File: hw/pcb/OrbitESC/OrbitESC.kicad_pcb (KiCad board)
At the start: 4 copper layers, 75 x 30 mm, 108 parts, among them J1 USB_C_Receptacle_USB2.0, J2 Micro_SD_Card_Det, J3 TermA, J4 TermB, J5 TermC, J6 CAN1, J7 Serial1, Q1 MCAC80N10Y, Q2 MCAC80N10Y, Q3 MCAC80N10Y, Q4 MCAC80N10Y, Q5 MCAC80N10Y, Q6 MCAC80N10Y, Q7 2N7002, U1 MCP2551-I-SN, U2 AT25SF081-SSHD-X, U3 24LC128, U4 STM32F446ZCHx, U5 DRV8300DRGER, U6 TSV994, U7 AP62200Z6-7, U8 AP2171W, U9 AP2120

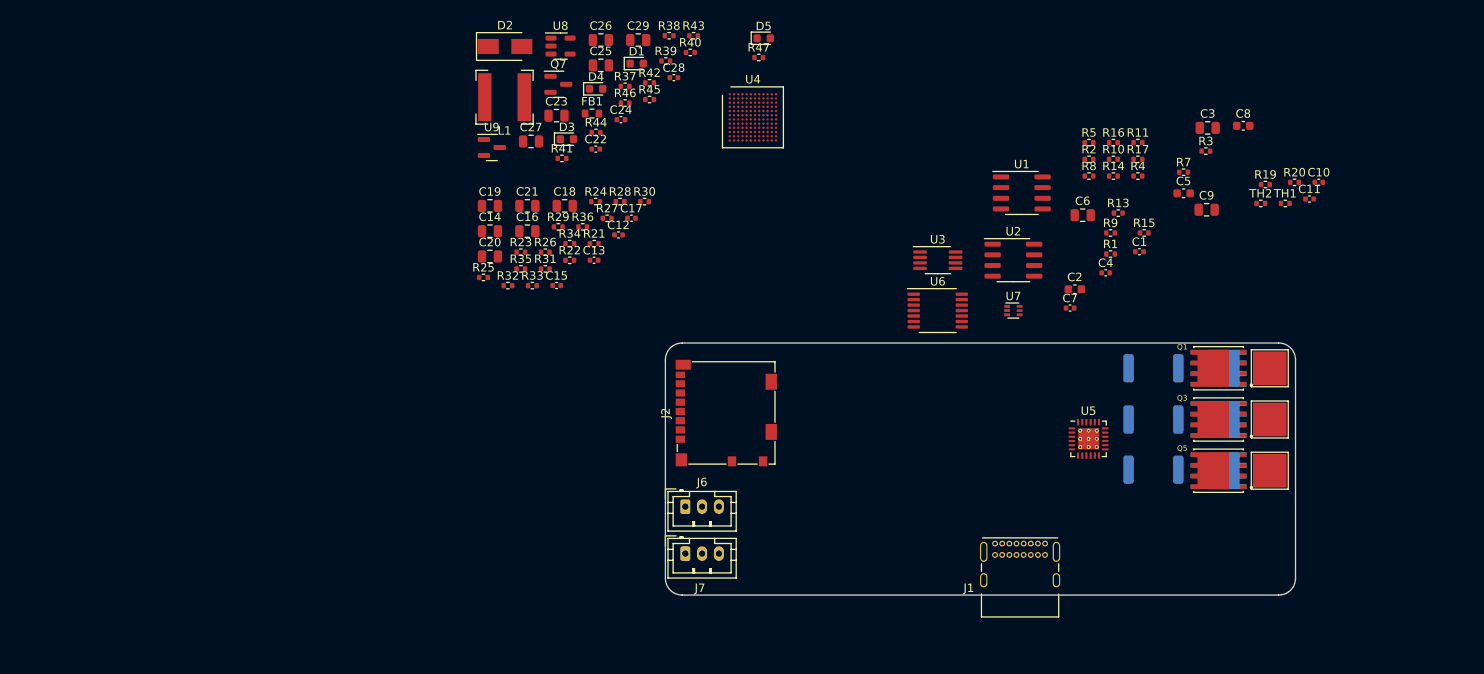
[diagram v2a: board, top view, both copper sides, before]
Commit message: Update PCB to match schematic
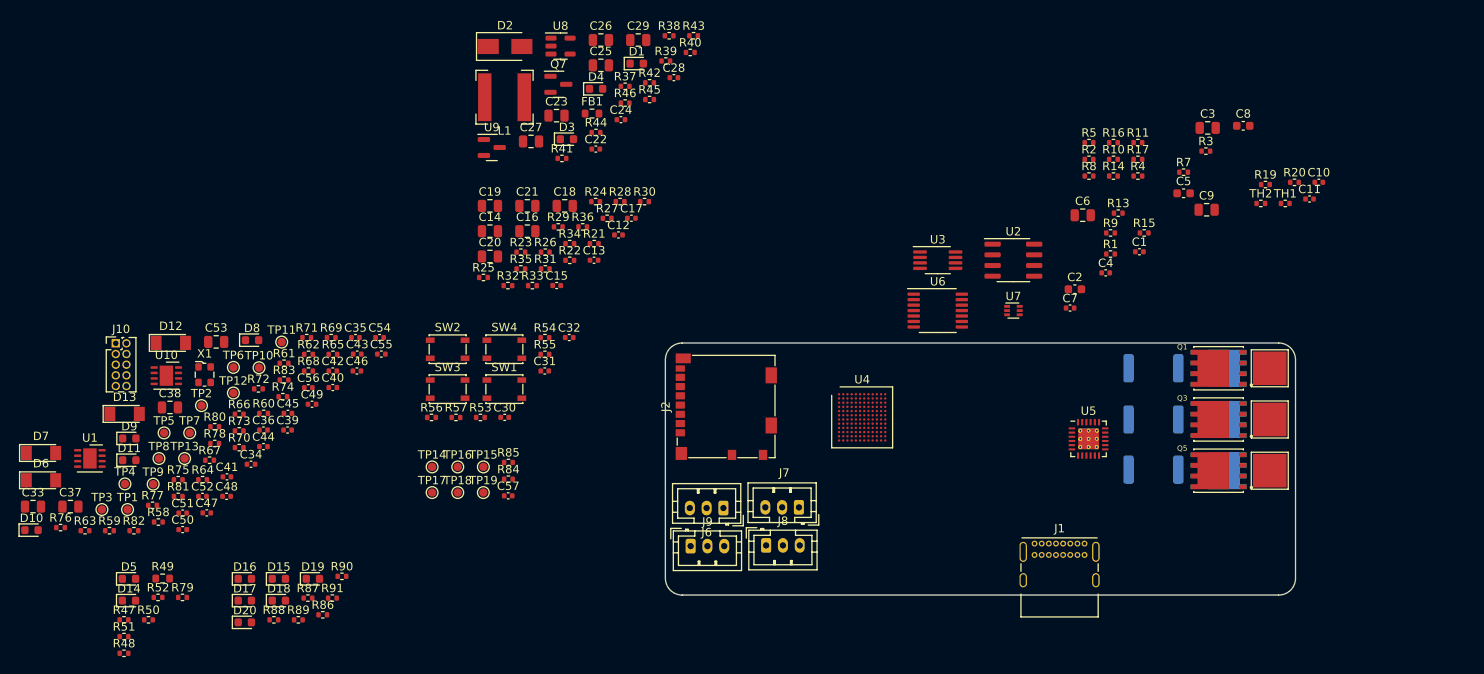
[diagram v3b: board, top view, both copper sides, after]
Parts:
- added C30: 100nF, Capacitor_SMD:C_0402_1005Metric, F.Cu at (84.5, 92.7)
- added C31: 100nF, Capacitor_SMD:C_0402_1005Metric, F.Cu at (89.2, 87.2)
- added C32: 100nF, Capacitor_SMD:C_0402_1005Metric, F.Cu at (92.1, 83.2)
- added C33: 2.2uF, Capacitor_SMD:C_0805_2012Metric, F.Cu at (28.3, 103.3)
- added C34: 100nF, Capacitor_SMD:C_0402_1005Metric, F.Cu at (54.3, 98.3)
- added C35: 100nF, Capacitor_SMD:C_0402_1005Metric, F.Cu at (66.7, 83.2)
- added C36: 100nF, Capacitor_SMD:C_0402_1005Metric, F.Cu at (55.7, 94.2)
- added C37: 2.2uF, Capacitor_SMD:C_0805_2012Metric, F.Cu at (32.8, 103.3)
- added C38: 2.2uF, Capacitor_SMD:C_0805_2012Metric, F.Cu at (44.6, 91.5)
- added C39: 100nF, Capacitor_SMD:C_0402_1005Metric, F.Cu at (58.6, 94.2)
- added C40: 100nF, Capacitor_SMD:C_0402_1005Metric, F.Cu at (64.0, 89.2)
- added C41: 100nF, Capacitor_SMD:C_0402_1005Metric, F.Cu at (51.4, 99.8)
- added C42: 100nF, Capacitor_SMD:C_0402_1005Metric, F.Cu at (64.0, 87.2)
- added C43: 100nF, Capacitor_SMD:C_0402_1005Metric, F.Cu at (66.9, 85.2)
- added C44: 100nF, Capacitor_SMD:C_0402_1005Metric, F.Cu at (55.7, 96.2)
- added C45: 100nF, Capacitor_SMD:C_0402_1005Metric, F.Cu at (58.7, 92.2)
- added C46: 100nF, Capacitor_SMD:C_0402_1005Metric, F.Cu at (66.9, 87.2)
- added C47: 100nF, Capacitor_SMD:C_0402_1005Metric, F.Cu at (49.0, 104.1)
- added C48: 100nF, Capacitor_SMD:C_0402_1005Metric, F.Cu at (51.4, 102.1)
- added C49: 100nF, Capacitor_SMD:C_0402_1005Metric, F.Cu at (61.5, 91.2)
- added C50: 100nF, Capacitor_SMD:C_0402_1005Metric, F.Cu at (46.1, 106.1)
- added C51: 100nF, Capacitor_SMD:C_0402_1005Metric, F.Cu at (46.1, 104.1)
- added C52: 100nF, Capacitor_SMD:C_0402_1005Metric, F.Cu at (48.5, 102.1)
- added C53: 2.2uF, Capacitor_SMD:C_0805_2012Metric, F.Cu at (50.1, 83.7)
- added C54: 100nF, Capacitor_SMD:C_0402_1005Metric, F.Cu at (69.6, 83.2)
- added C55: 100nF, Capacitor_SMD:C_0402_1005Metric, F.Cu at (69.8, 85.2)
- added C56: 100nF, Capacitor_SMD:C_0402_1005Metric, F.Cu at (61.1, 89.2)
- added C57: 100nF, Capacitor_SMD:C_0402_1005Metric, F.Cu at (84.9, 102.0)
- added D10: Yellow LED, Diode_SMD:D_0603_1608Metric, F.Cu at (28.1, 106.1)
- added D11: Yellow LED, Diode_SMD:D_0603_1608Metric, F.Cu at (39.8, 97.8)
- added D12: 3.3V, Diode_SMD:D_MiniMELF, F.Cu at (44.7, 83.8)
- added D13: 3.3V, Diode_SMD:D_MiniMELF, F.Cu at (39.2, 92.3)
- added D14: Yellow LED, Diode_SMD:D_0603_1608Metric, F.Cu at (39.7, 114.5)
- added D15: Green LED, Diode_SMD:D_0603_1608Metric, F.Cu at (57.6, 111.9)
- added D16: Blue LED, Diode_SMD:D_0603_1608Metric, F.Cu at (53.5, 111.9)
- added D17: Blue LED, Diode_SMD:D_0603_1608Metric, F.Cu at (53.5, 114.5)
- added D18: Green LED, Diode_SMD:D_0603_1608Metric, F.Cu at (57.6, 114.5)
- added D19: Blue LED, Diode_SMD:D_0603_1608Metric, F.Cu at (61.6, 111.9)
- added D20: Red LED, Diode_SMD:D_0603_1608Metric, F.Cu at (53.5, 117.1)
- added D6: 3.3V, Diode_SMD:D_MiniMELF, F.Cu at (29.3, 100.2)
- added D7: 3.3V, Diode_SMD:D_MiniMELF, F.Cu at (29.3, 97.0)
- added D8: Yellow LED, Diode_SMD:D_0603_1608Metric, F.Cu at (54.4, 83.5)
- added D9: Yellow LED, Diode_SMD:D_0603_1608Metric, F.Cu at (39.8, 95.2)
- added J10: ~, Connector_PinHeader_1.27mm:PinHeader_2x05_P1.27mm_Vertical, F.Cu at (38.2, 83.9)
- added J8: Serial2, Connector_JST:JST_PH_B3B-PH-K_1x03_P2.00mm_Vertical, F.Cu at (115.6, 108.0)
- added J9: CAN2, Connector_JST:JST_PH_B3B-PH-K_1x03_P2.00mm_Vertical, F.Cu at (106.6, 108.0)
- added R48: 33k, Resistor_SMD:R_0402_1005Metric, F.Cu at (39.1, 120.8)
- added R49: 82k, Resistor_SMD:R_0603_1608Metric, F.Cu at (43.7, 111.9)
- added R50: 1.5k, Resistor_SMD:R_0402_1005Metric, F.Cu at (42.1, 116.8)
- added R51: 5.1k, Resistor_SMD:R_0402_1005Metric, F.Cu at (39.1, 118.8)
- added R52: 5.1k, Resistor_SMD:R_0402_1005Metric, F.Cu at (43.2, 114.1)
- added R53: 10k, Resistor_SMD:R_0402_1005Metric, F.Cu at (81.6, 92.7)
- added R54: 10k, Resistor_SMD:R_0402_1005Metric, F.Cu at (89.2, 83.2)
- added R55: 10k, Resistor_SMD:R_0402_1005Metric, F.Cu at (89.2, 85.2)
- added R56: 10k, Resistor_SMD:R_0402_1005Metric, F.Cu at (75.7, 92.7)
- added R57: 10k, Resistor_SMD:R_0402_1005Metric, F.Cu at (78.7, 92.7)
- added R58: 1.5k, Resistor_SMD:R_0402_1005Metric, F.Cu at (43.2, 105.2)
- added R59: 1.5k, Resistor_SMD:R_0402_1005Metric, F.Cu at (37.4, 106.2)
- added R60: 1.5k, Resistor_SMD:R_0402_1005Metric, F.Cu at (55.8, 92.2)
- added R61: 1.5k, Resistor_SMD:R_0402_1005Metric, F.Cu at (58.2, 86.3)
- added R62: 120, Resistor_SMD:R_0402_1005Metric, F.Cu at (61.1, 85.2)
- added R63: 120, Resistor_SMD:R_0402_1005Metric, F.Cu at (34.5, 106.2)
- added R64: 1.5k, Resistor_SMD:R_0402_1005Metric, F.Cu at (48.5, 100.1)
- added R65: 1.5k, Resistor_SMD:R_0402_1005Metric, F.Cu at (64.0, 85.2)
- added R66: 1.5k, Resistor_SMD:R_0402_1005Metric, F.Cu at (52.9, 92.3)
- added R67: 1.5k, Resistor_SMD:R_0402_1005Metric, F.Cu at (49.3, 97.8)
- added R68: 1.5k, Resistor_SMD:R_0402_1005Metric, F.Cu at (61.1, 87.2)
- added R69: 10k, Resistor_SMD:R_0402_1005Metric, F.Cu at (63.8, 83.2)
- added R70: 10k, Resistor_SMD:R_0402_1005Metric, F.Cu at (52.9, 96.3)
- added R71: 10k, Resistor_SMD:R_0402_1005Metric, F.Cu at (60.9, 83.2)
- added R72: 39k, Resistor_SMD:R_0402_1005Metric, F.Cu at (55.1, 89.3)
- added R73: 39k, Resistor_SMD:R_0402_1005Metric, F.Cu at (52.9, 94.3)
- added R74: 39k, Resistor_SMD:R_0402_1005Metric, F.Cu at (58.1, 90.2)
- added R75: 39k, Resistor_SMD:R_0402_1005Metric, F.Cu at (45.6, 100.1)
- added R76: 39k, Resistor_SMD:R_0402_1005Metric, F.Cu at (31.6, 105.8)
- added R77: 1.5k, Resistor_SMD:R_0402_1005Metric, F.Cu at (42.5, 103.2)
- added R78: 1.5k, Resistor_SMD:R_0402_1005Metric, F.Cu at (49.9, 95.8)
- added R79: 1.5k, Resistor_SMD:R_0402_1005Metric, F.Cu at (46.1, 114.1)
- added R80: 100k, Resistor_SMD:R_0402_1005Metric, F.Cu at (49.9, 93.8)
- added R81: 100k, Resistor_SMD:R_0402_1005Metric, F.Cu at (45.6, 102.1)
- added R82: 100k, Resistor_SMD:R_0402_1005Metric, F.Cu at (40.3, 106.2)
- added R83: 100k, Resistor_SMD:R_0402_1005Metric, F.Cu at (58.2, 88.3)
- added R84: 10k, Resistor_SMD:R_0402_1005Metric, F.Cu at (84.9, 100.1)
- added R85: 10k, Resistor_SMD:R_0402_1005Metric, F.Cu at (84.9, 98.1)
- added R86: 10k, Resistor_SMD:R_0402_1005Metric, F.Cu at (62.8, 116.2)
- added R87: 200, Resistor_SMD:R_0402_1005Metric, F.Cu at (61.0, 114.2)
- added R88: 200, Resistor_SMD:R_0402_1005Metric, F.Cu at (57.0, 116.8)
- added R89: 10k, Resistor_SMD:R_0402_1005Metric, F.Cu at (59.9, 116.8)
- added R90: 200, Resistor_SMD:R_0402_1005Metric, F.Cu at (65.1, 111.6)
- added R91: 1.5k, Resistor_SMD:R_0402_1005Metric, F.Cu at (63.9, 114.2)
- added SW1: Reset, Button_Switch_SMD:SW_SPST_PTS810, F.Cu at (84.4, 89.3)
- added SW2: User, Button_Switch_SMD:SW_SPST_PTS810, F.Cu at (77.7, 84.6)
- added SW3: Boot, Button_Switch_SMD:SW_SPST_PTS810, F.Cu at (77.7, 89.3)
- added SW4: Break, Button_Switch_SMD:SW_SPST_PTS810, F.Cu at (84.4, 84.6)
- added TP1: SDIO_CMD, TestPoint:TestPoint_Pad_D1.0mm, F.Cu at (39.6, 103.7)
- added TP10: NOR_SCK, TestPoint:TestPoint_Pad_D1.0mm, F.Cu at (55.2, 86.8)
- added TP11: EEPROM_SDA, TestPoint:TestPoint_Pad_D1.0mm, F.Cu at (57.9, 83.8)
- added TP12: EEPROM_SCL, TestPoint:TestPoint_Pad_D1.0mm, F.Cu at (52.2, 89.8)
- added TP13: NOR_MISO, TestPoint:TestPoint_Pad_D1.0mm, F.Cu at (46.4, 97.6)
- added TP14: AH, TestPoint:TestPoint_Pad_D1.0mm, F.Cu at (75.8, 98.6)
- added TP15: AL, TestPoint:TestPoint_Pad_D1.0mm, F.Cu at (81.9, 98.6)
- added TP16: BH, TestPoint:TestPoint_Pad_D1.0mm, F.Cu at (78.9, 98.6)
- added TP17: BL, TestPoint:TestPoint_Pad_D1.0mm, F.Cu at (75.8, 101.7)
- added TP18: CH, TestPoint:TestPoint_Pad_D1.0mm, F.Cu at (78.9, 101.7)
- added TP19: CL, TestPoint:TestPoint_Pad_D1.0mm, F.Cu at (81.9, 101.7)
- added TP2: SDIO_DATA_2, TestPoint:TestPoint_Pad_D1.0mm, F.Cu at (48.4, 91.3)
- added TP3: SDIO_DATA_0, TestPoint:TestPoint_Pad_D1.0mm, F.Cu at (36.5, 103.7)
- added TP4: SDIO_CARD_DETECT, TestPoint:TestPoint_Pad_D1.0mm, F.Cu at (39.3, 100.6)
- added TP5: NOR_nCS, TestPoint:TestPoint_Pad_D1.0mm, F.Cu at (43.9, 94.6)
- added TP6: SDIO_DATA_3, TestPoint:TestPoint_Pad_D1.0mm, F.Cu at (52.2, 86.8)
- added TP7: SDIO_CLK, TestPoint:TestPoint_Pad_D1.0mm, F.Cu at (47.0, 94.6)
- added TP8: SDIO_DATA_1, TestPoint:TestPoint_Pad_D1.0mm, F.Cu at (43.3, 97.6)
- added TP9: NOR_MOSI, TestPoint:TestPoint_Pad_D1.0mm, F.Cu at (42.6, 100.7)
- added U10: TLE9250X, Package_SON:HVSON-8-1EP_3x3mm_P0.65mm_EP1.6x2.4mm, F.Cu at (44.2, 87.8)
- added X1: ECS-2520MV-240-BN, Oscillator:Oscillator_SMD_ECS_2520MV-xxx-xx-4Pin_2.5x2.0mm, F.Cu at (48.7, 87.6)
- U1: value MCP2551-I-SN -> TLE9250X; footprint Package_SO:SOIC-8_3.9x4.9mm_P1.27mm -> Package_SON:HVSON-8-1EP_3x3mm_P0.65mm_EP1.6x2.4mm
- moved U1 115.3 mm to (35.1, 97.6)
- moved R47 100.9 mm to (39.1, 116.8)
- moved D5 99.2 mm to (39.7, 111.9)
- moved U4 38.0 mm to (127.0, 92.7)
- moved J7 14.6 mm to (119.5, 103.4), turned to 180 degrees
- moved J1 4.70 mm to (147.5, 107.7)
- moved J6 4.54 mm to (110.5, 103.5), turned to 180 degrees
- moved J2 0.76 mm to (110.8, 91.4)
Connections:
- C1 pad 1: /Outputs and Shunts/VA_FB -> /MCU/MOTOR_VA
- C10 pad 1: /Outputs and Shunts/TempA -> /MCU/TEMP_VA
- C10 pad 2: GNDD -> GND
- C11 pad 1: /Outputs and Shunts/TempB -> /MCU/TEMP_VB
- C11 pad 2: GNDD -> GND
- C13 pad 1: /Power Stage/VS -> /MCU/INPUT_VOLTAGE
- C13 pad 2: GNDD -> GND
- C15 pad 1: /Power Stage/VL -> /MCU/+3V3_VOLTAGE
- C15 pad 2: GNDD -> GND
- C22 pad 1: GNDD -> GND
- C23 pad 2: GNDD -> GND
- C25 pad 2: GNDD -> GND
- C26 pad 2: GNDD -> GND
- C27 pad 1: GNDD -> GND
- C28 pad 2: GNDD -> GND
- C29 pad 1: GNDD -> GND
- C4 pad 1: /Outputs and Shunts/VB_FB -> /MCU/MOTOR_VB
- C7 pad 1: /Outputs and Shunts/VC_FB -> /MCU/MOTOR_VC
- D1 pad 1: GNDD -> GND
- D2 pad 2: GNDD -> GND
- D3 pad 1: GNDD -> GND
- D4 pad 1: GNDD -> GND
- D5 pad 1: unconnected-(D5-Pad1) -> GND
- D5 pad 2: unconnected-(D5-Pad2) -> Net-(D5-Pad2)
- J1 pad A1: Net-(J1-PadA1) -> GND
- J1 pad A12: Net-(J1-PadA1) -> GND
- J1 pad A4: Net-(J1-PadA4) -> VBUS
- J1 pad A5: unconnected-(J1-PadA5) -> Net-(J1-PadA5)
- J1 pad A6: unconnected-(J1-PadA6) -> USB_D+
- J1 pad A7: unconnected-(J1-PadA7) -> USB_D-
- J1 pad A9: Net-(J1-PadA4) -> VBUS
- J1 pad B1: Net-(J1-PadA1) -> GND
- J1 pad B12: Net-(J1-PadA1) -> GND
- J1 pad B4: Net-(J1-PadA4) -> VBUS
- J1 pad B5: unconnected-(J1-PadB5) -> Net-(J1-PadB5)
- J1 pad B6: unconnected-(J1-PadB6) -> USB_D+
- J1 pad B7: unconnected-(J1-PadB7) -> USB_D-
- J1 pad B9: Net-(J1-PadA4) -> VBUS
- J1 pad S1: unconnected-(J1-PadS1) -> GND
- J2 pad 1: unconnected-(J2-Pad1) -> SDIO_DATA_2
- J2 pad 10: unconnected-(J2-Pad10) -> SDIO_CARD_DETECT
- J2 pad 11: unconnected-(J2-Pad11) -> GND
- J2 pad 2: unconnected-(J2-Pad2) -> SDIO_DATA_3
- J2 pad 3: unconnected-(J2-Pad3) -> SDIO_CMD
- J2 pad 4: unconnected-(J2-Pad4) -> +3.3V
- J2 pad 5: unconnected-(J2-Pad5) -> SDIO_CLK
- J2 pad 6: unconnected-(J2-Pad6) -> GND
- J2 pad 7: unconnected-(J2-Pad7) -> SDIO_DATA_0
- J2 pad 8: unconnected-(J2-Pad8) -> SDIO_DATA_1
- J2 pad 9: unconnected-(J2-Pad9) -> GND
- J6 pad 1: unconnected-(J6-Pad1) -> Net-(J6-Pad1)
- J6 pad 2: unconnected-(J6-Pad2) -> GND
- J6 pad 3: unconnected-(J6-Pad3) -> Net-(J6-Pad3)
- J7 pad 1: unconnected-(J7-Pad1) -> Net-(D6-Pad1)
- J7 pad 2: unconnected-(J7-Pad2) -> Net-(D12-Pad1)
- J7 pad 3: unconnected-(J7-Pad3) -> GND
- Q7 pad 2: GNDD -> GND
- R1 pad 2: /Outputs and Shunts/VA_FB -> /MCU/MOTOR_VA
- R13 pad 2: /Outputs and Shunts/VB_FB -> /MCU/MOTOR_VB
- R15 pad 1: /Outputs and Shunts/VB_FB -> /MCU/MOTOR_VB
- R19 pad 2: /Outputs and Shunts/VC_FB -> /MCU/MOTOR_VC
- R20 pad 1: /Outputs and Shunts/VC_FB -> /MCU/MOTOR_VC
- R23 pad 1: /Power Stage/VS -> /MCU/INPUT_VOLTAGE
- R24 pad 1: /Power Stage/VS -> /MCU/INPUT_VOLTAGE
- R24 pad 2: GNDD -> GND
- R25 pad 1: /Power Stage/IC -> /MCU/MOTOR_IC
- R27 pad 2: Net-(U6-Pad3) -> ISenseVRef
- R29 pad 1: /Power Stage/VL -> /MCU/+3V3_VOLTAGE
- R3 pad 1: /Outputs and Shunts/VA_FB -> /MCU/MOTOR_VA
- R30 pad 1: GNDD -> GND
- R30 pad 2: /Power Stage/VL -> /MCU/+3V3_VOLTAGE
- R31 pad 1: /Power Stage/IB -> /MCU/MOTOR_IB
- R33 pad 2: Net-(U6-Pad10) -> ISenseVRef
- R34 pad 1: /Power Stage/IA -> /MCU/MOTOR_IA
- R36 pad 2: Net-(U6-Pad5) -> ISenseVRef
- R38 pad 1: GNDD -> GND
- R41 pad 1: GNDD -> GND
- R47 pad 1: unconnected-(R47-Pad1) -> VBUS
- R47 pad 2: unconnected-(R47-Pad2) -> Net-(D5-Pad2)
- R7 pad 1: /Outputs and Shunts/TempA -> /MCU/TEMP_VA
- R7 pad 2: GNDD -> GND
- R9 pad 1: /Outputs and Shunts/TempB -> /MCU/TEMP_VB
- R9 pad 2: GNDD -> GND
- TH1 pad 2: /Outputs and Shunts/TempA -> /MCU/TEMP_VA
- TH2 pad 2: /Outputs and Shunts/TempB -> /MCU/TEMP_VB
- U1 pad 1: unconnected-(U1-Pad1) -> CAN1_TXD
- U1 pad 2: unconnected-(U1-Pad2) -> GND
- U1 pad 3: unconnected-(U1-Pad3) -> +5V
- U1 pad 4: unconnected-(U1-Pad4) -> CAN1_RXD
- U1 pad 5: unconnected-(U1-Pad5) -> +3.3V
- U1 pad 6: unconnected-(U1-Pad6) -> Net-(J6-Pad3)
- U1 pad 7: unconnected-(U1-Pad7) -> Net-(J6-Pad1)
- U2 pad 1: unconnected-(U2-Pad1) -> NOR_nCS
- U2 pad 2: unconnected-(U2-Pad2) -> NOR_MISO
- U2 pad 3: unconnected-(U2-Pad3) -> +3.3V
- U2 pad 4: unconnected-(U2-Pad4) -> GND
- U2 pad 5: unconnected-(U2-Pad5) -> NOR_MOSI
- U2 pad 6: unconnected-(U2-Pad6) -> NOR_SCK
- U2 pad 7: unconnected-(U2-Pad7) -> +3.3V
- U2 pad 8: unconnected-(U2-Pad8) -> +3.3V
- U3 pad 1: unconnected-(U3-Pad1) -> GND
- U3 pad 2: unconnected-(U3-Pad2) -> GND
- U3 pad 3: unconnected-(U3-Pad3) -> GND
- U3 pad 4: unconnected-(U3-Pad4) -> GND
- U3 pad 5: unconnected-(U3-Pad5) -> EEPROM_SDA
- U3 pad 6: unconnected-(U3-Pad6) -> EEPROM_SCL
- U3 pad 7: unconnected-(U3-Pad7) -> GND
- U3 pad 8: unconnected-(U3-Pad8) -> +3.3V
- U4 pad A1: unconnected-(U4-PadA1) -> HEARTBEAT_LED
- U4 pad A10: unconnected-(U4-PadA10) -> JTAG_TDI
- U4 pad A11: unconnected-(U4-PadA11) -> JTAG_TCLK
- U4 pad A12: unconnected-(U4-PadA12) -> JTAG_TMS
- U4 pad A2: unconnected-(U4-PadA2) -> USER_BTN
- U4 pad A3: unconnected-(U4-PadA3) -> FAULT_LED
- U4 pad A4: unconnected-(U4-PadA4) -> ARMED_LED
- U4 pad A5: unconnected-(U4-PadA5) -> CAN1_ACTV_LED
- U4 pad A7: unconnected-(U4-PadA7) -> JTAG_TDO
- U4 pad A8: unconnected-(U4-PadA8) -> SERIAL1_IN
- U4 pad B10: unconnected-(U4-PadB10) -> SDIO_DATA_3
- U4 pad B11: unconnected-(U4-PadB11) -> SDIO_DATA_2
- U4 pad B12: unconnected-(U4-PadB12) -> USB_D+
- U4 pad B2: unconnected-(U4-PadB2) -> STATUS_0_LED
- U4 pad B3: unconnected-(U4-PadB3) -> STATUS_1_LED
- U4 pad B4: unconnected-(U4-PadB4) -> STATUS_2_LED
- U4 pad B5: unconnected-(U4-PadB5) -> CAN1_TXD
- U4 pad B6: unconnected-(U4-PadB6) -> CAN2_RXD
- U4 pad B7: unconnected-(U4-PadB7) -> CAN2_ACTV_LED
- U4 pad B8: unconnected-(U4-PadB8) -> SERIAL1_ACTV_LED
- U4 pad B9: unconnected-(U4-PadB9) -> SERIAL1_OUT
- U4 pad C10: unconnected-(U4-PadC10) -> SDIO_CLK
- U4 pad C11: unconnected-(U4-PadC11) -> +3.3V
- U4 pad C12: unconnected-(U4-PadC12) -> USB_D-
- U4 pad C2: unconnected-(U4-PadC2) -> +3.3V
- U4 pad C3: unconnected-(U4-PadC3) -> EEPROM_SDA
- U4 pad C4: unconnected-(U4-PadC4) -> EEPROM_SCL
- U4 pad C5: unconnected-(U4-PadC5) -> CAN1_RXD
- U4 pad C6: unconnected-(U4-PadC6) -> CAN2_TXD
- U4 pad C7: unconnected-(U4-PadC7) -> SERIAL2_OUT
- U4 pad D1: unconnected-(U4-PadD1) -> OSC
- U4 pad D10: unconnected-(U4-PadD10) -> SDIO_CARD_DETECT
- U4 pad D11: unconnected-(U4-PadD11) -> USB_ACTV_LED
- U4 pad D12: unconnected-(U4-PadD12) -> USB_Detect
- U4 pad D2: unconnected-(U4-PadD2) -> GND
- U4 pad D3: unconnected-(U4-PadD3) -> +3.3V
- U4 pad D5: unconnected-(U4-PadD5) -> BOOT0
- U4 pad D7: unconnected-(U4-PadD7) -> SERIAL2_ACTV_LED
- U4 pad E11: unconnected-(U4-PadE11) -> SDIO_DATA_1
- U4 pad E12: unconnected-(U4-PadE12) -> USB_ENUM
- U4 pad E2: unconnected-(U4-PadE2) -> /MCU/TEMP_VA
- U4 pad E5: unconnected-(U4-PadE5) -> +3.3V
- U4 pad E6: unconnected-(U4-PadE6) -> GND
- U4 pad E7: unconnected-(U4-PadE7) -> GND
- U4 pad E8: unconnected-(U4-PadE8) -> SERIAL2_IN
- U4 pad E9: unconnected-(U4-PadE9) -> SDIO_CMD
- U4 pad F1: unconnected-(U4-PadF1) -> nRESET
- U4 pad F10: unconnected-(U4-PadF10) -> +3.3V
- U4 pad F11: unconnected-(U4-PadF11) -> SDIO_DATA_0
- U4 pad F4: unconnected-(U4-PadF4) -> +3.3V
- U4 pad F5: unconnected-(U4-PadF5) -> +3.3V
- U4 pad F6: unconnected-(U4-PadF6) -> +3.3V
- U4 pad F7: unconnected-(U4-PadF7) -> +3.3V
- U4 pad F8: unconnected-(U4-PadF8) -> +3.3V
- U4 pad F9: unconnected-(U4-PadF9) -> +3.3V
- U4 pad G1: unconnected-(U4-PadG1) -> /MCU/+3V3_VOLTAGE
- U4 pad G10: unconnected-(U4-PadG10) -> GND
- U4 pad G2: unconnected-(U4-PadG2) -> /MCU/TEMP_VB
- U4 pad G4: unconnected-(U4-PadG4) -> GND
- U4 pad G5: unconnected-(U4-PadG5) -> +3.3V
- U4 pad G6: unconnected-(U4-PadG6) -> +3.3V
- U4 pad G7: unconnected-(U4-PadG7) -> +3.3V
- U4 pad G8: unconnected-(U4-PadG8) -> GND
- U4 pad G9: unconnected-(U4-PadG9) -> Net-(C38-Pad2)
- U4 pad H1: unconnected-(U4-PadH1) -> /MCU/+5V0_VOLTAGE
- U4 pad H5: unconnected-(U4-PadH5) -> Net-(R69-Pad2)
- U4 pad H6: unconnected-(U4-PadH6) -> GND
- U4 pad H7: unconnected-(U4-PadH7) -> Net-(C37-Pad2)
- U4 pad H8: unconnected-(U4-PadH8) -> /MCU/GATE_DRIVE_BH
- U4 pad J1: unconnected-(U4-PadJ1) -> GND
- U4 pad J2: unconnected-(U4-PadJ2) -> /MCU/INPUT_VOLTAGE
- U4 pad J3: unconnected-(U4-PadJ3) -> /MCU/MOTOR_VA
- U4 pad J5: unconnected-(U4-PadJ5) -> BOOT1
- U4 pad J7: unconnected-(U4-PadJ7) -> /MCU/GATE_DRIVE_BL
- U4 pad J8: unconnected-(U4-PadJ8) -> /MCU/GATE_DRIVE_CL
- U4 pad K1: unconnected-(U4-PadK1) -> GND
- U4 pad K2: unconnected-(U4-PadK2) -> /MCU/MOTOR_IA
- U4 pad K3: unconnected-(U4-PadK3) -> /MCU/MOTOR_VB
- U4 pad K7: unconnected-(U4-PadK7) -> /MCU/GATE_DRIVE_AH
- U4 pad K8: unconnected-(U4-PadK8) -> /MCU/GATE_DRIVE_CH
- U4 pad L1: unconnected-(U4-PadL1) -> +3.3VADC
- U4 pad L11: unconnected-(U4-PadL11) -> NOR_MISO
- U4 pad L12: unconnected-(U4-PadL12) -> NOR_MOSI
- U4 pad L2: unconnected-(U4-PadL2) -> /MCU/MOTOR_IB
- U4 pad L3: unconnected-(U4-PadL3) -> /MCU/MOTOR_VC
- U4 pad L7: unconnected-(U4-PadL7) -> /MCU/GATE_DRIVE_AL
- U4 pad M1: unconnected-(U4-PadM1) -> +3.3VADC
- U4 pad M11: unconnected-(U4-PadM11) -> NOR_nCS
- U4 pad M12: unconnected-(U4-PadM12) -> NOR_SCK
- U4 pad M2: unconnected-(U4-PadM2) -> /MCU/MOTOR_IC
- U4 pad M8: unconnected-(U4-PadM8) -> TIM1_BREAK
- U5 pad 1: /Power Stage/AL -> /MCU/GATE_DRIVE_AL
- U5 pad 2: /Power Stage/BL -> /MCU/GATE_DRIVE_BL
- U5 pad 22: /Power Stage/AH -> /MCU/GATE_DRIVE_AH
- U5 pad 23: /Power Stage/BH -> /MCU/GATE_DRIVE_BH
- U5 pad 24: /Power Stage/CH -> /MCU/GATE_DRIVE_CH
- U5 pad 25: (no net) -> GND
- U5 pad 3: /Power Stage/CL -> /MCU/GATE_DRIVE_CL
- U5 pad 7: (no net) -> unconnected-(U5-Pad7)
- U5 pad 8: (no net) -> unconnected-(U5-Pad8)
- U6 pad 1: /Power Stage/IC -> /MCU/MOTOR_IC
- U6 pad 10: Net-(U6-Pad10) -> ISenseVRef
- U6 pad 3: Net-(U6-Pad3) -> ISenseVRef
- U6 pad 5: Net-(U6-Pad5) -> ISenseVRef
- U6 pad 7: /Power Stage/IA -> /MCU/MOTOR_IA
- U6 pad 8: /Power Stage/IB -> /MCU/MOTOR_IB
- U7 pad 3: GNDD -> GND
- U8 pad 2: GNDD -> GND
- U9 pad 1: GNDD -> GND

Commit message: Start routing power stage
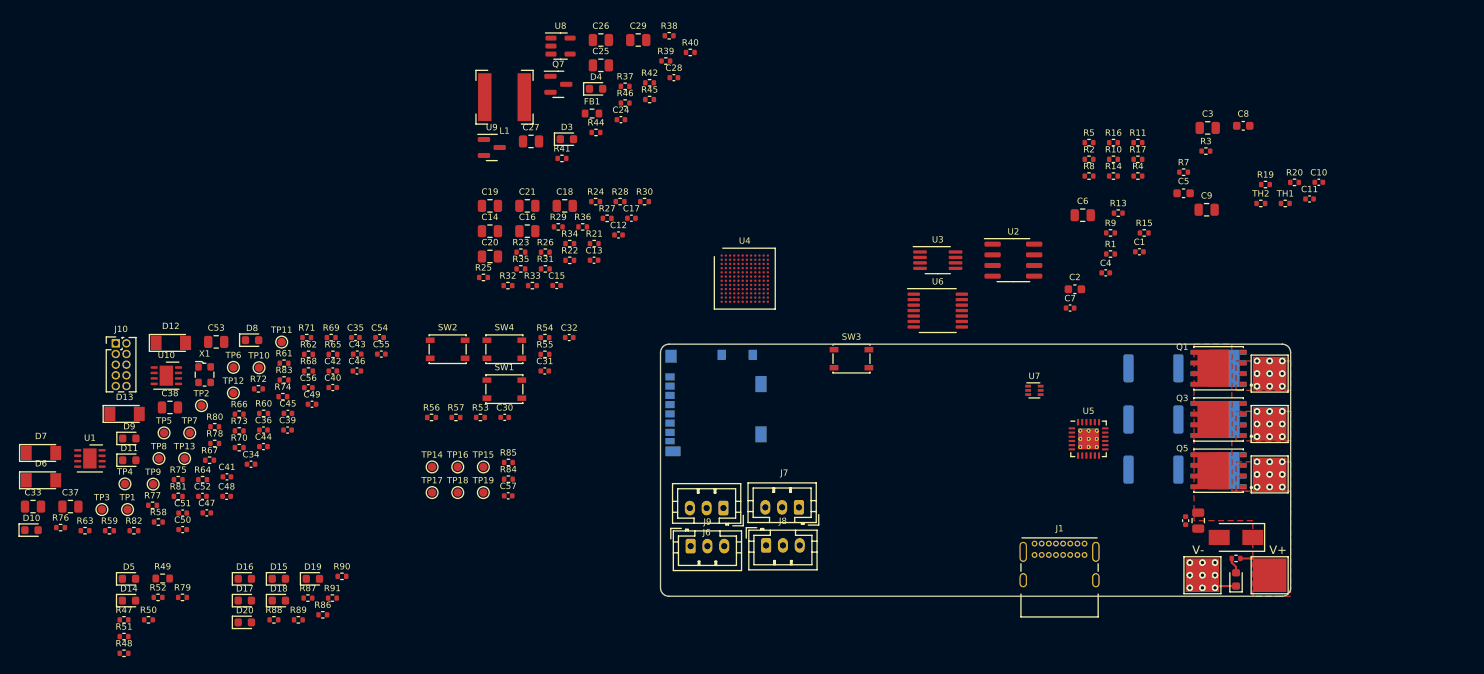
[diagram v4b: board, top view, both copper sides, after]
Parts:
- added J11: VDC, TestPoint:TestPoint_Pad_4.0x4.0mm, F.Cu at (175.5, 111.5)
- added J12: GND, TestPoint:TestPoint_Pad_4.0x4.0mm, F.Cu at (167.5, 111.5)
- J2: moved to B.Cu
- moved D2 104.8 mm to (171.5, 107.0), turned to 180 degrees
- moved D1 94.1 mm to (171.5, 112.0), turned to 90 degrees
- moved C23 90.3 mm to (167.0, 105.0), turned to -90 degrees
- moved R43 89.7 mm to (171.5, 109.5), turned to 180 degrees
- moved C22 83.0 mm to (165.5, 105.0), turned to 90 degrees
- moved SW3 48.2 mm to (125.7, 85.7)
- moved U4 21.6 mm to (113.0, 76.2)
- moved U7 9.82 mm to (147.5, 89.5)
- moved J2 1.30 mm to (109.6, 91.0), turned to -90 degrees
- moved J3 0.63 mm to (175.5, 87.5)
- moved J4 0.54 mm to (175.5, 93.5)
- moved J5 0.44 mm to (175.5, 99.5)
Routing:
- net VDC: track 0.00 -> 4.32 mm
- net GND: track 0.00 -> 2.59 mm, vias 0 -> 9
- net Net-(D1-Pad2): track 0.00 -> 1.92 mm
- net /Outputs and Shunts/SH_C: vias 0 -> 9
- net /Outputs and Shunts/SH_B: vias 0 -> 9
- net /Outputs and Shunts/SH_A: vias 0 -> 9
- added copper zone on F.Cu, net /Outputs and Shunts/SH_A
- added copper zone on F.Cu, net /Outputs and Shunts/SH_B
- added copper zone on F.Cu, net /Outputs and Shunts/SH_C
- added copper zone on In1.Cu, net GND
- added copper zone on F.Cu, net VDC
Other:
- outline, holes or cut-outs redrawn
- board text added: "V+"
- board text added: "V-"

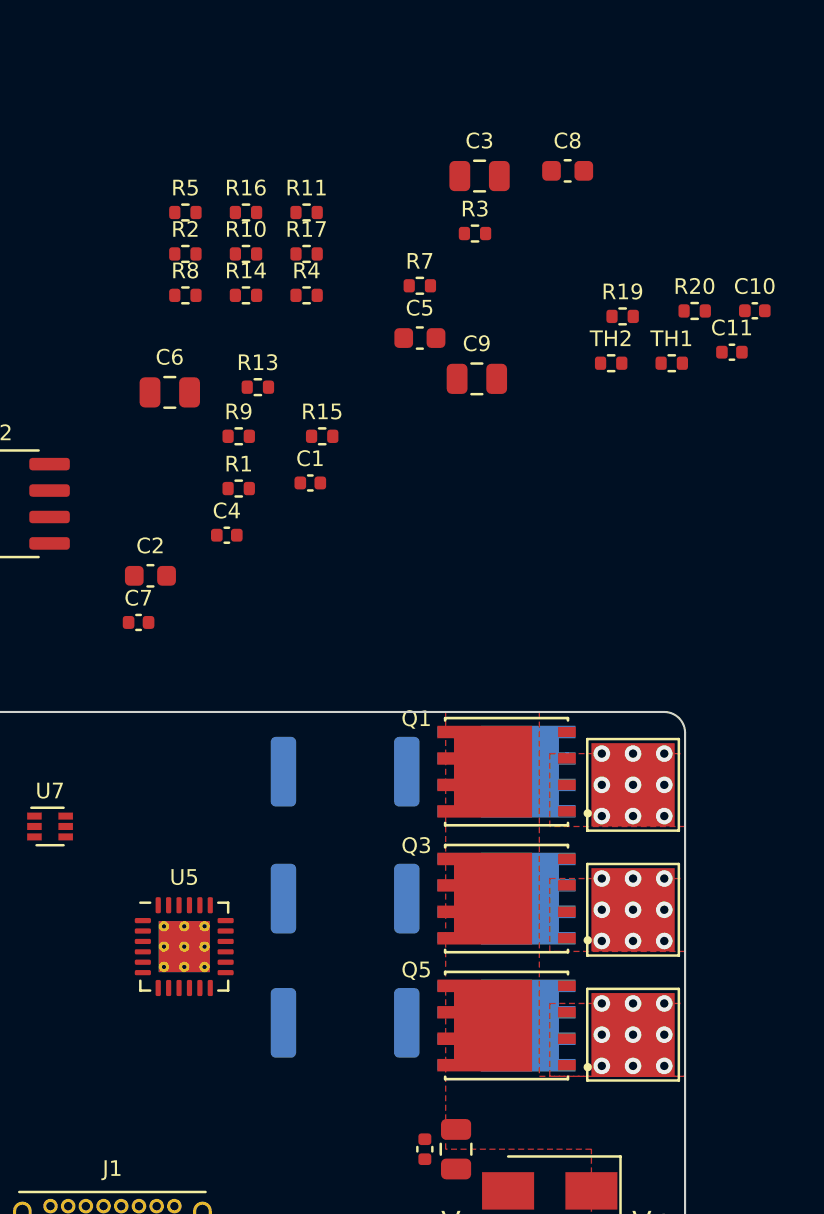
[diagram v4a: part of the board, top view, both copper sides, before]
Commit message: Route more of the power stage
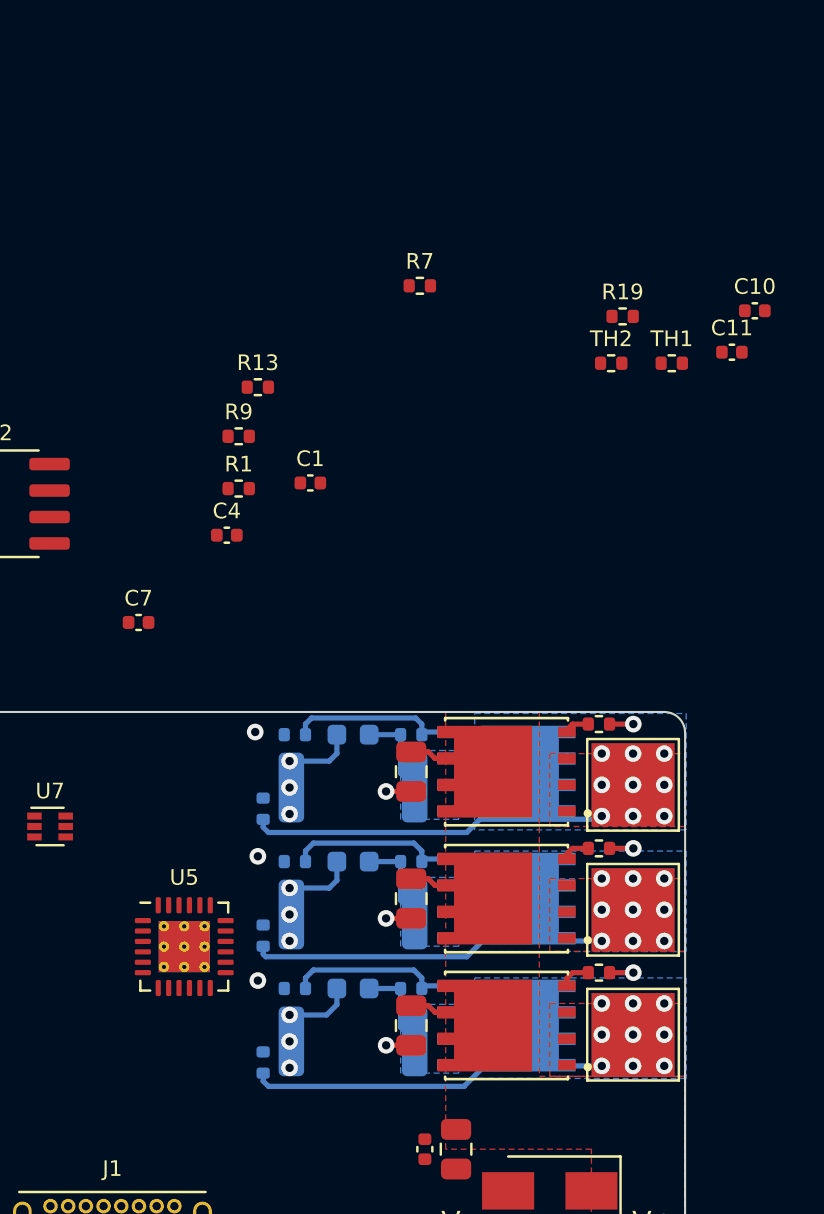
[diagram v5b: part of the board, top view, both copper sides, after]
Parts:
- C2, C5, C8, R10, R11, R15, R16, R17, R20, R3, R4, R5: moved to B.Cu
- moved R20 41.6 mm to (157.7, 100.8), turned to -90 degrees
- moved C8 40.6 mm to (162.1, 97.3), turned to 180 degrees
- moved R16 37.3 mm to (159.3, 97.3)
- moved R14 36.7 mm to (173.9, 96.5), turned to 180 degrees
- moved R17 35.6 mm to (164.8, 97.3), turned to 180 degrees
- moved R8 33.2 mm to (173.9, 90.6), turned to 180 degrees
- moved R11 31.6 mm to (164.8, 91.2), turned to 180 degrees
- moved C9 31.2 mm to (164.8, 99.1), turned to -90 degrees
- moved R2 30.1 mm to (173.9, 84.6), turned to 180 degrees
- moved R3 29.4 mm to (157.7, 88.6), turned to -90 degrees
- moved R10 29.3 mm to (159.3, 91.2)
- moved C3 28.8 mm to (164.8, 86.9), turned to -90 degrees
- moved R5 27.3 mm to (164.8, 85.1), turned to 180 degrees
- moved C6 26.9 mm to (164.8, 93.0), turned to -90 degrees
- moved C5 25.3 mm to (162.1, 91.2), turned to 180 degrees
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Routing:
- net /Outputs and Shunts/GDH_A: track 0.00 -> 19.5 mm, vias 0 -> 2
- net /Outputs and Shunts/GDH_C: track 0.00 -> 19.3 mm, vias 0 -> 2
- net /Outputs and Shunts/GDH_B: track 0.00 -> 19.3 mm, vias 0 -> 2
- net /Outputs and Shunts/SH_C: track 0.00 -> 17.2 mm
- net /Outputs and Shunts/SH_A: track 0.00 -> 17.1 mm
- net /Outputs and Shunts/SH_B: track 0.00 -> 17.0 mm
- net GND: track 2.59 -> 16.4 mm, vias 9 -> 21
- net Net-(Q4-Pad2): track 0.00 -> 8.13 mm
- net Net-(Q6-Pad2): track 0.00 -> 8.13 mm
- net Net-(Q2-Pad2): track 0.00 -> 8.05 mm
- net VDC: track 4.32 -> 9.67 mm
- net /Outputs and Shunts/C_ISENSE_P: track 0.00 -> 4.33 mm
- net /Outputs and Shunts/B_ISENSE_P: track 0.00 -> 4.33 mm
- net /Outputs and Shunts/A_ISENSE_P: track 0.00 -> 4.33 mm
- net Net-(Q5-Pad2): track 0.00 -> 1.51 mm
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- added copper zone on B.Cu, net /Outputs and Shunts/A_ISENSE_P
- added copper zone on B.Cu, net /Outputs and Shunts/B_ISENSE_P
- added copper zone on B.Cu, net /Outputs and Shunts/C_ISENSE_P
- added copper zone on B.Cu, net /Outputs and Shunts/SH_A
- added copper zone on B.Cu, net /Outputs and Shunts/SH_B
- added copper zone on B.Cu, net /Outputs and Shunts/SH_C
